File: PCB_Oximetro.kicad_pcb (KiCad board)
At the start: 2 copper layers, 61.2 x 57.9 mm, 14 parts, among them J1 Conn_01x05, J2 Conn_01x08, J3 USB_B_Micro, SW1 SW_Push, U3 LM1117MP-3.3, U5 ESP32-DEVKIT-V1

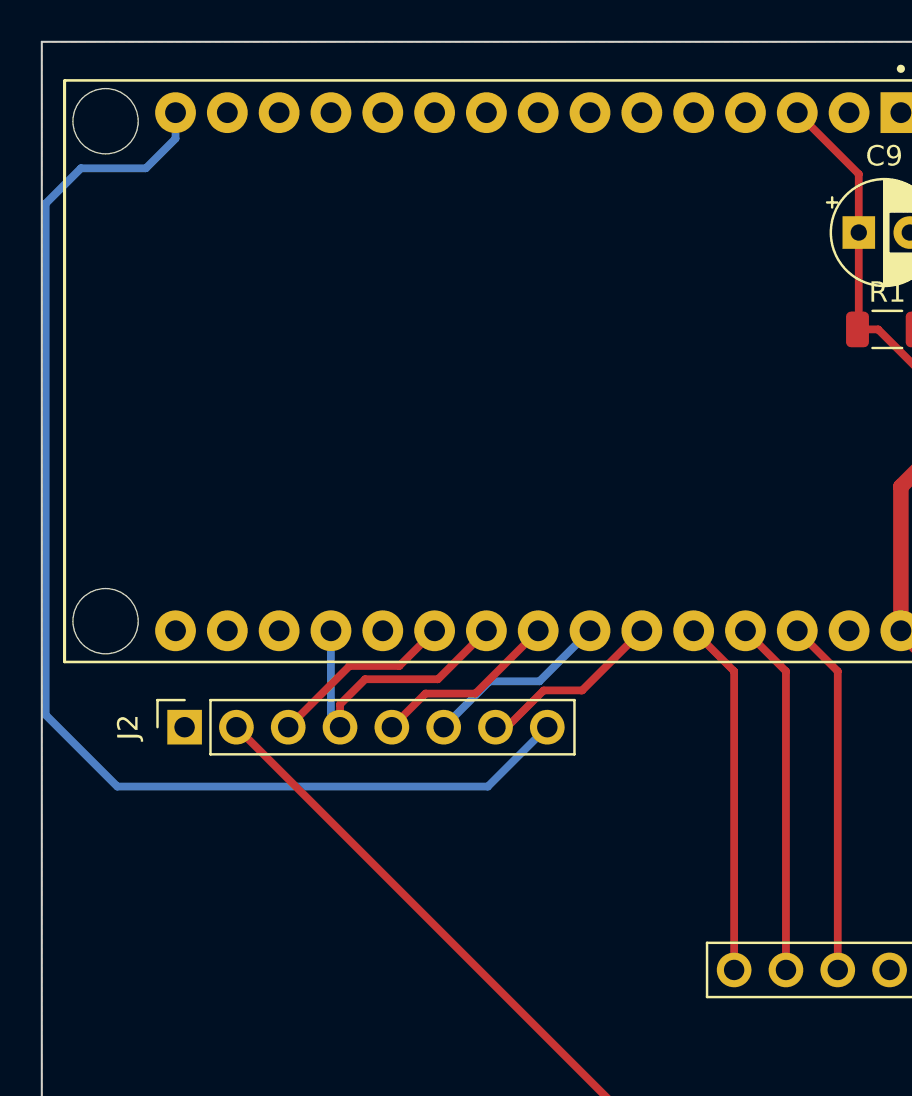
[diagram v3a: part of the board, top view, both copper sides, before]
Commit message: GPIO12 change
GPIO12 change because of ESP32 boot
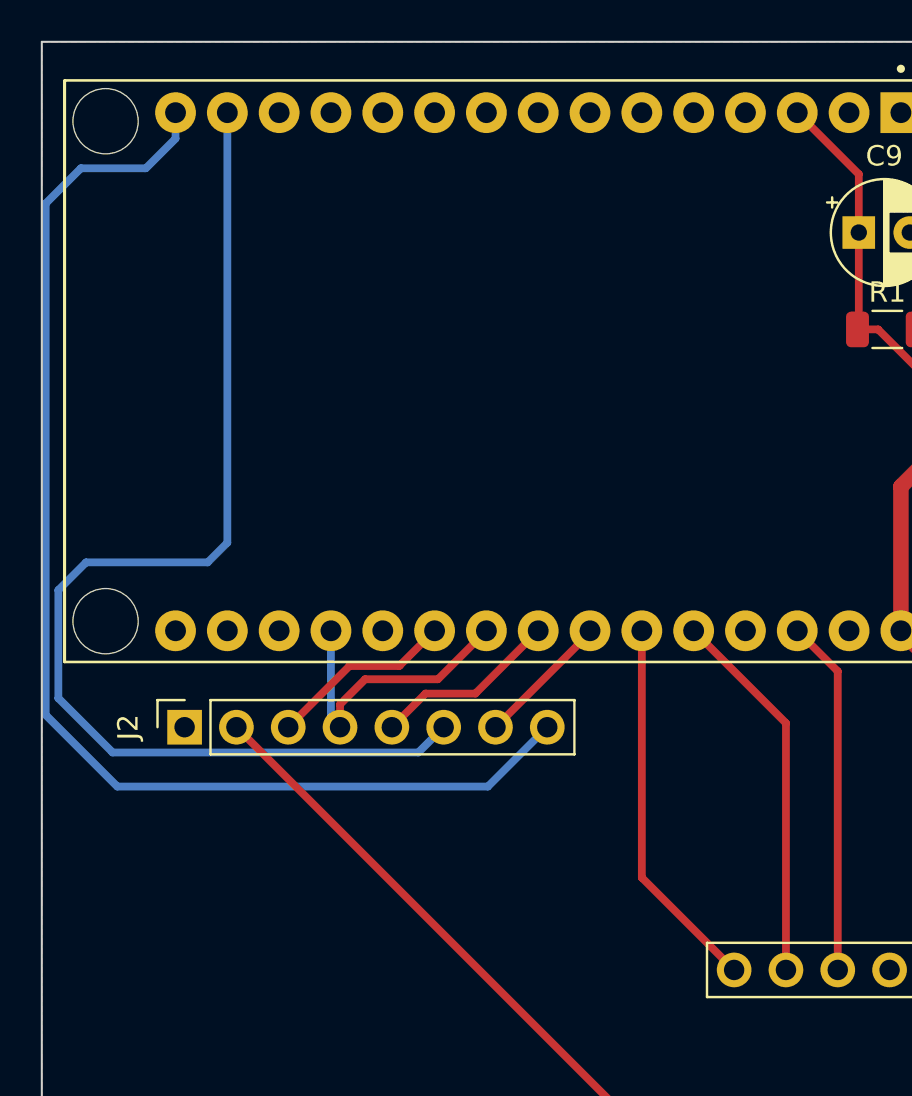
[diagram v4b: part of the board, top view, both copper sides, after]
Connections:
- U5 pad 14: unconnected-(U5-D22-Pad14) -> DC
- U5 pad 24: DC -> CS
- U5 pad 25: CS -> INT
- U5 pad 26: INT -> SDA
- U5 pad 27: SDA -> unconnected-(U5-D12-Pad27)
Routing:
- net DC: track 9.13 -> 56.1 mm
- net CS: track 9.13 -> 7.30 mm
- net INT: track 17.4 -> 18.5 mm
- net unconnected-(U5-D12-Pad27): track 0.00 -> 0.68 mm
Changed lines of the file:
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@@
   (net 23 "unconnected-(U5-3V3-Pad1)")
   (net 24 "Net-(R2-Pad2)")
-  (net 25 "unconnected-(U5-D22-Pad14)")
+  (net 25 "unconnected-(U5-D12-Pad27)")
   (net 26 "unconnected-(U5-D19-Pad10)")
   (net 27 "unconnected-(U5-TX2-Pad7)")
@@
       (net 18 "unconnected-(U5-TX0-Pad13)") (pinfunction "TX0") (pintype "output+no_connect") (solder_mask_margin 0.102))
     (pad "14" thru_hole circle (at -12.7 17.505 270) (size 2 2) (drill 1.02) (layers "*.Cu" "*.Mask")
-      (net 25 "unconnected-(U5-D22-Pad14)") (pinfunction "D22") (pintype "bidirectional+no_connect") (solder_mask_margin 0.102))
+      (net 7 "DC") (pinfunction "D22") (pintype "bidirectional") (solder_mask_margin 0.102))
     (pad "15" thru_hole circle (at -12.7 20.045 270) (size 2 2) (drill 1.02) (layers "*.Cu" "*.Mask")
       (net 9 "BLK") (pinfunction "D23") (pintype "bidirectional") (solder_mask_margin 0.102))
@@
       (net 6 "RESET") (pinfunction "D25") (pintype "bidirectional") (solder_mask_margin 0.102))
     (pad "24" thru_hole circle (at 12.7 -0.275 270) (size 2 2) (drill 1.02) (layers "*.Cu" "*.Mask")
-      (net 7 "DC") (pinfunction "D26") (pintype "bidirectional") (solder_mask_margin 0.102))
+      (net 8 "CS") (pinfunction "D26") (pintype "bidirectional") (solder_mask_margin 0.102))
     (pad "25" thru_hole circle (at 12.7 -2.815 270) (size 2 2) (drill 1.02) (layers "*.Cu" "*.Mask")
-      (net 8 "CS") (pinfunction "D27") (pintype "bidirectional") (solder_mask_margin 0.102))
+      (net 12 "INT") (pinfunction "D27") (pintype "bidirectional") (solder_mask_margin 0.102))
     (pad "26" thru_hole circle (at 12.7 -5.355 270) (size 2 2) (drill 1.02) (layers "*.Cu" "*.Mask")
-      (net 12 "INT") (pinfunction "D14") (pintype "bidirectional") (solder_mask_margin 0.102))
+      (net 11 "SDA") (pinfunction "D14") (pintype "bidirectional") (solder_mask_margin 0.102))
     (pad "27" thru_hole circle (at 12.7 -7.895 270) (size 2 2) (drill 1.02) (layers "*.Cu" "*.Mask")
-      (net 11 "SDA") (pinfunction "D12") (pintype "bidirectional") (solder_mask_margin 0.102))
+      (net 25 "unconnected-(U5-D12-Pad27)") (pinfunction "D12") (pintype "bidirectional+no_connect") (solder_mask_margin 0.102))
     (pad "28" thru_hole circle (at 12.7 -10.435 270) (size 2 2) (drill 1.02) (layers "*.Cu" "*.Mask")
       (net 10 "SCL") (pinfunction "D13") (pintype "bidirectional") (solder_mask_margin 0.102))
@@
   (segment (start 113.06 91.3) (end 114.71 89.65) (width 0.381) (layer "F.Cu") (net 6))
   (segment (start 114.71 89.65) (end 117.1575 89.65) (width 0.381) (layer "F.Cu") (net 6))
-  (segment (start 120.2975 89.05) (end 117.85 89.05) (width 0.381) (layer "B.Cu") (net 7))
-  (segment (start 117.85 89.05) (end 115.6 91.3) (width 0.381) (layer "B.Cu") (net 7))
-  (segment (start 122.775 86.5725) (end 120.2975 89.05) (width 0.381) (layer "B.Cu") (net 7))
-  (segment (start 122.3875 89.5) (end 125.315 86.5725) (width 0.381) (layer "F.Cu") (net 8))
-  (segment (start 118.7 91.3) (end 120.5 89.5) (width 0.381) (layer "F.Cu") (net 8))
+  (segment (start 96.71 84.58) (end 96.71 89.88) (width 0.381) (layer "B.Cu") (net 7))
+  (segment (start 99.3705 92.5405) (end 114.3595 92.5405) (width 0.381) (layer "B.Cu") (net 7))
+  (segment (start 104.995 82.255) (end 104.03 83.22) (width 0.381) (layer "B.Cu") (net 7))
+  (segment (start 96.71 89.88) (end 99.3705 92.5405) (width 0.381) (layer "B.Cu") (net 7))
+  (segment (start 104.995 61.1725) (end 104.995 82.255) (width 0.381) (layer "B.Cu") (net 7))
+  (segment (start 114.3595 92.5405) (end 115.6 91.3) (width 0.381) (layer "B.Cu") (net 7))
+  (segment (start 98.07 83.22) (end 96.71 84.58) (width 0.381) (layer "B.Cu") (net 7))
+  (segment (start 104.03 83.22) (end 98.07 83.22) (width 0.381) (layer "B.Cu") (net 7))
+  (segment (start 122.775 86.665) (end 122.775 86.5725) (width 0.381) (layer "F.Cu") (net 8))
+  (segment (start 118.14 91.2075) (end 118.14 91.3) (width 0.25) (layer "F.Cu") (net 8))
+  (segment (start 118.14 91.3) (end 122.775 86.665) (width 0.381) (layer "F.Cu") (net 8))
   (segment (start 118.14 91.3) (end 118.7 91.3) (width 0.381) (layer "F.Cu") (net 8))
-  (segment (start 120.5 89.5) (end 122.3875 89.5) (width 0.381) (layer "F.Cu") (net 8))
   (segment (start 96.0905 90.7) (end 99.6 94.2095) (width 0.381) (layer "B.Cu") (net 9))
   (segment (start 97.818092 63.9) (end 96.0905 65.627592) (width 0.381) (layer "B.Cu") (net 9))
@@
   (segment (start 134.92 103.2) (end 134.92 88.5575) (width 0.381) (layer "F.Cu") (net 10))
   (segment (start 134.92 88.5575) (end 132.935 86.5725) (width 0.381) (layer "F.Cu") (net 10))
-  (segment (start 130.395 86.5725) (end 132.38 88.5575) (width 0.381) (layer "F.Cu") (net 11))
-  (segment (start 132.38 88.5575) (end 132.38 103.2) (width 0.381) (layer "F.Cu") (net 11))
-  (segment (start 131.0725 86.5725) (end 130.395 86.5725) (width 0.381) (layer "F.Cu") (net 11))
-  (segment (start 129.84 88.5575) (end 129.84 103.2) (width 0.381) (layer "F.Cu") (net 12))
-  (segment (start 127.855 86.5725) (end 129.84 88.5575) (width 0.381) (layer "F.Cu") (net 12))
+  (segment (start 132.38 91.0975) (end 127.855 86.5725) (width 0.381) (layer "F.Cu") (net 11))
+  (segment (start 132.38 103.2) (end 132.38 91.0975) (width 0.381) (layer "F.Cu") (net 11))
+  (segment (start 125.315 86.5725) (end 125.315 98.675) (width 0.381) (layer "F.Cu") (net 12))
+  (segment (start 125.315 98.675) (end 129.84 103.2) (width 0.381) (layer "F.Cu") (net 12))
   (segment (start 135.8875 71.8) (end 136.901 71.8) (width 0.381) (layer "F.Cu") (net 13))
   (segment (start 135.95 64.1875) (end 132.935 61.1725) (width 0.381) (layer "F.Cu") (net 13))
@@
   (segment (start 154.847 82.4155) (end 155.0375 82.225) (width 0.381) (layer "F.Cu") (net 24))
   (segment (start 149.5655 82.4155) (end 154.847 82.4155) (width 0.381) (layer "F.Cu") (net 24))
+  (segment (start 131.0725 86.5725) (end 130.395 86.5725) (width 0.381) (layer "F.Cu") (net 25))
   (zone (net 1) (net_name "GNDPWR") (layer "F.Cu") (name "GND") (hatch edge 0.5)
     (connect_pads thru_hole_only (clearance 0.4))

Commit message: BTT pin
Changed BTT pin because of boot
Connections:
- U5 pad 3: BTT -> unconnected-(U5-D15-Pad3)
- U5 pad 6: unconnected-(U5-RX2-Pad6) -> BTT
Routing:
- net BTT: track 37.2 -> 43.2 mm
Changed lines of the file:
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@@
   (net 26 "unconnected-(U5-D19-Pad10)")
   (net 27 "unconnected-(U5-TX2-Pad7)")
-  (net 28 "unconnected-(U5-RX2-Pad6)")
+  (net 28 "unconnected-(U5-D15-Pad3)")
   (net 29 "unconnected-(U5-D4-Pad5)")
   (net 30 "unconnected-(U5-D2-Pad4)")
@@
       (net 1 "GNDPWR") (pinfunction "GND") (pintype "power_in") (solder_mask_margin 0.102))
     (pad "3" thru_hole circle (at -12.7 -10.435 270) (size 2 2) (drill 1.02) (layers "*.Cu" "*.Mask")
-      (net 13 "BTT") (pinfunction "D15") (pintype "bidirectional") (solder_mask_margin 0.102))
+      (net 28 "unconnected-(U5-D15-Pad3)") (pinfunction "D15") (pintype "bidirectional+no_connect") (solder_mask_margin 0.102))
     (pad "4" thru_hole circle (at -12.7 -7.895 270) (size 2 2) (drill 1.02) (layers "*.Cu" "*.Mask")
       (net 30 "unconnected-(U5-D2-Pad4)") (pinfunction "D2") (pintype "bidirectional+no_connect") (solder_mask_margin 0.102))
@@
       (net 29 "unconnected-(U5-D4-Pad5)") (pinfunction "D4") (pintype "bidirectional+no_connect") (solder_mask_margin 0.102))
     (pad "6" thru_hole circle (at -12.7 -2.815 270) (size 2 2) (drill 1.02) (layers "*.Cu" "*.Mask")
-      (net 28 "unconnected-(U5-RX2-Pad6)") (pinfunction "RX2") (pintype "input+no_connect") (solder_mask_margin 0.102))
+      (net 13 "BTT") (pinfunction "RX2") (pintype "input") (solder_mask_margin 0.102))
     (pad "7" thru_hole circle (at -12.7 -0.275 270) (size 2 2) (drill 1.02) (layers "*.Cu" "*.Mask")
       (net 27 "unconnected-(U5-TX2-Pad7)") (pinfunction "TX2") (pintype "output+no_connect") (solder_mask_margin 0.102))
@@
   (segment (start 125.315 98.675) (end 129.84 103.2) (width 0.381) (layer "F.Cu") (net 12))
   (segment (start 135.8875 71.8) (end 136.901 71.8) (width 0.381) (layer "F.Cu") (net 13))
-  (segment (start 135.95 64.1875) (end 132.935 61.1725) (width 0.381) (layer "F.Cu") (net 13))
   (segment (start 135.8875 71.8) (end 135.95 71.7375) (width 0.381) (layer "F.Cu") (net 13))
+  (segment (start 135.95 67.05) (end 133.34 64.44) (width 0.381) (layer "F.Cu") (net 13))
   (segment (start 135.95 71.7375) (end 135.95 67.05) (width 0.381) (layer "F.Cu") (net 13))
+  (segment (start 133.34 64.44) (end 128.5825 64.44) (width 0.381) (layer "F.Cu") (net 13))
   (segment (start 136.901 71.8) (end 148.951 83.85) (width 0.381) (layer "F.Cu") (net 13))
   (segment (start 148.951 83.85) (end 152.1625 83.85) (width 0.381) (layer "F.Cu") (net 13))
+  (segment (start 128.5825 64.44) (end 125.315 61.1725) (width 0.381) (layer "F.Cu") (net 13))
   (segment (start 152.1625 83.85) (end 155.0375 86.725) (width 0.381) (layer "F.Cu") (net 13))
-  (segment (start 135.95 67.05) (end 135.95 64.1875) (width 0.381) (layer "F.Cu") (net 13))
   (segment (start 125.034888 110.894888) (end 105.44 91.3) (width 0.381) (layer "F.Cu") (net 22))
   (segment (start 148.934888 110.894888) (end 125.034888 110.894888) (width 0.381) (layer "F.Cu") (net 22))

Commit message: 1.0.0v
Plot Gerbers files
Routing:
- net 3V3: track 66.8 -> 78.9 mm
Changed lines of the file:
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@@
     (pad_to_mask_clearance 0)
     (pcbplotparams
-      (layerselection 0x00010fc_ffffffff)
+      (layerselection 0x0001000_fffffffe)
       (plot_on_all_layers_selection 0x0000000_00000000)
       (disableapertmacros false)
@@
       (dashed_line_gap_ratio 3.000000)
       (svgprecision 4)
-      (plotframeref false)
+      (plotframeref true)
       (viasonmask false)
       (mode 1)
@@
       (outputformat 1)
       (mirror false)
-      (drillshape 1)
+      (drillshape 0)
       (scaleselection 1)
       (outputdirectory "")
@@
     (fp_line (start 1.6 0.8) (end -1.6 0.8)
       (stroke (width 0.1) (type solid)) (layer "F.Fab"))
-    (pad "1" smd roundrect (at -1.4625 0) (size 1.125 1.75) (layers "F.Cu" "F.Paste" "F.Mask") (roundrect_rratio 0.222222)
+    (pad "1" smd roundrect (at -1.4625 0) (size 1.125 1.75) (layers "F.Cu" "F.Paste" "F.Mask") (roundrect_rratio 0.2222222222)
       (net 13 "BTT") (pintype "passive"))
-    (pad "2" smd roundrect (at 1.4625 0) (size 1.125 1.75) (layers "F.Cu" "F.Paste" "F.Mask") (roundrect_rratio 0.222222)
+    (pad "2" smd roundrect (at 1.4625 0) (size 1.125 1.75) (layers "F.Cu" "F.Paste" "F.Mask") (roundrect_rratio 0.2222222222)
       (net 1 "GNDPWR") (pintype "passive"))
     (model "${KICAD6_3DMODEL_DIR}/Resistor_SMD.3dshapes/R_1206_3216Metric.wrl"
@@
     (fp_line (start 1.6 0.8) (end -1.6 0.8)
       (stroke (width 0.1) (type solid)) (layer "F.Fab"))
-    (pad "1" smd roundrect (at -1.475 0 270) (size 1.15 1.8) (layers "F.Cu" "F.Paste" "F.Mask") (roundrect_rratio 0.217391)
+    (pad "1" smd roundrect (at -1.475 0 270) (size 1.15 1.8) (layers "F.Cu" "F.Paste" "F.Mask") (roundrect_rratio 0.2173913043)
       (net 22 "3V3") (pintype "passive"))
-    (pad "2" smd roundrect (at 1.475 0 270) (size 1.15 1.8) (layers "F.Cu" "F.Paste" "F.Mask") (roundrect_rratio 0.217391)
+    (pad "2" smd roundrect (at 1.475 0 270) (size 1.15 1.8) (layers "F.Cu" "F.Paste" "F.Mask") (roundrect_rratio 0.2173913043)
       (net 1 "GNDPWR") (pintype "passive"))
     (model "${KICAD6_3DMODEL_DIR}/Capacitor_SMD.3dshapes/C_1206_3216Metric.wrl"
@@
     (fp_line (start 1.6 0.8) (end -1.6 0.8)
       (stroke (width 0.1) (type solid)) (layer "F.Fab"))
-    (pad "1" smd roundrect (at -1.475 0) (size 1.15 1.8) (layers "F.Cu" "F.Paste" "F.Mask") (roundrect_rratio 0.217391)
+    (pad "1" smd roundrect (at -1.475 0) (size 1.15 1.8) (layers "F.Cu" "F.Paste" "F.Mask") (roundrect_rratio 0.2173913043)
       (net 2 "+5V") (pintype "passive"))
-    (pad "2" smd roundrect (at 1.475 0) (size 1.15 1.8) (layers "F.Cu" "F.Paste" "F.Mask") (roundrect_rratio 0.217391)
+    (pad "2" smd roundrect (at 1.475 0) (size 1.15 1.8) (layers "F.Cu" "F.Paste" "F.Mask") (roundrect_rratio 0.2173913043)
       (net 1 "GNDPWR") (pintype "passive"))
     (model "${KICAD6_3DMODEL_DIR}/Capacitor_SMD.3dshapes/C_1206_3216Metric.wrl"
@@
     (fp_line (start 1.6 0.8) (end -1.6 0.8)
       (stroke (width 0.1) (type solid)) (layer "F.Fab"))
-    (pad "1" smd roundrect (at -1.4625 0 90) (size 1.125 1.75) (layers "F.Cu" "F.Paste" "F.Mask") (roundrect_rratio 0.222222)
+    (pad "1" smd roundrect (at -1.4625 0 90) (size 1.125 1.75) (layers "F.Cu" "F.Paste" "F.Mask") (roundrect_rratio 0.2222222222)
       (net 2 "+5V") (pintype "passive"))
-    (pad "2" smd roundrect (at 1.4625 0 90) (size 1.125 1.75) (layers "F.Cu" "F.Paste" "F.Mask") (roundrect_rratio 0.222222)
+    (pad "2" smd roundrect (at 1.4625 0 90) (size 1.125 1.75) (layers "F.Cu" "F.Paste" "F.Mask") (roundrect_rratio 0.2222222222)
       (net 24 "Net-(R2-Pad2)") (pintype "passive"))
     (model "${KICAD6_3DMODEL_DIR}/Resistor_SMD.3dshapes/R_1206_3216Metric.wrl"
@@
   (segment (start 128.5825 64.44) (end 125.315 61.1725) (width 0.381) (layer "F.Cu") (net 13))
   (segment (start 152.1625 83.85) (end 155.0375 86.725) (width 0.381) (layer "F.Cu") (net 13))
+  (segment (start 148.934888 110.894888) (end 147.694888 110.894888) (width 0.381) (layer "F.Cu") (net 22))
   (segment (start 125.034888 110.894888) (end 105.44 91.3) (width 0.381) (layer "F.Cu") (net 22))
   (segment (start 148.934888 110.894888) (end 125.034888 110.894888) (width 0.381) (layer "F.Cu") (net 22))
@@
   (segment (start 152.030112 110.894888) (end 153.25 109.675) (width 0.762) (layer "F.Cu") (net 22))
   (segment (start 148.934888 110.894888) (end 152.030112 110.894888) (width 0.762) (layer "F.Cu") (net 22))
+  (segment (start 147.694888 110.894888) (end 140 103.2) (width 0.381) (layer "F.Cu") (net 22))
   (segment (start 152.475 109.675) (end 150.15 107.35) (width 0.762) (layer "F.Cu") (net 22))
   (segment (start 149.4 82.25) (end 149.5655 82.4155) (width 0.381) (layer "F.Cu") (net 24))

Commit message: Update MISO
MISO Removed for compatibility
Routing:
- net MISO: track 14.7 -> 10.4 mm
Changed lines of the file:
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@@
   (segment (start 110.52 90.18) (end 110.52 91.3) (width 0.381) (layer "F.Cu") (net 5))
   (segment (start 110.075 90.855) (end 110.52 91.3) (width 0.381) (layer "B.Cu") (net 5))
-  (segment (start 110.075 86.5725) (end 110.075 90.855) (width 0.381) (layer "B.Cu") (net 5))
   (segment (start 117.1575 89.65) (end 120.235 86.5725) (width 0.381) (layer "F.Cu") (net 6))
   (segment (start 113.06 91.3) (end 114.71 89.65) (width 0.381) (layer "F.Cu") (net 6))

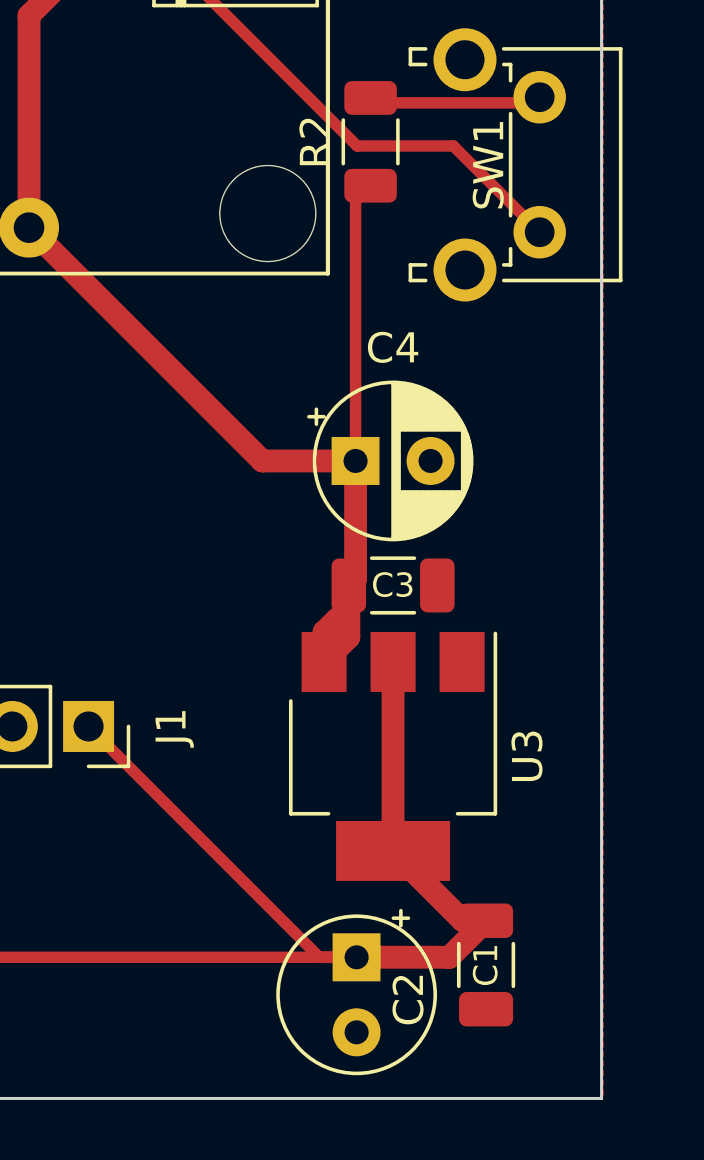
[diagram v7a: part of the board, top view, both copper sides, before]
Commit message: Capacitor size change
Changed capacitor smd 1206 to 0805 because of availibility
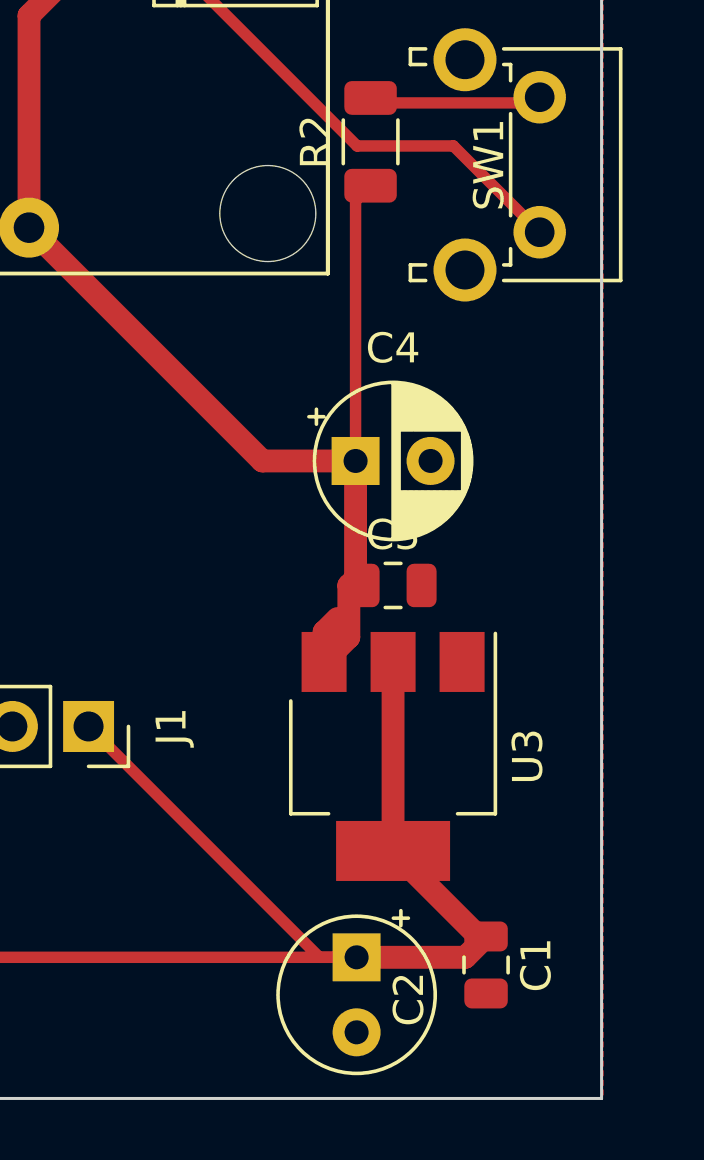
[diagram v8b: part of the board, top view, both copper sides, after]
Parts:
- C1, C3: footprint Capacitor_SMD:C_1206_3216Metric -> Capacitor_SMD:C_0805_2012Metric
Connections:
- J2 pad 4: MISO -> MOSI
- U5 pad 19: MISO -> unconnected-(U5-D34-Pad19)
- U5 pad 22: MISO -> MOSI
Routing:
- net MOSI: track 0.00 -> 10.4 mm
- net MISO: track 10.4 -> 0.00 mm
